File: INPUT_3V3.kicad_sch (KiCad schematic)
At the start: 3 parts

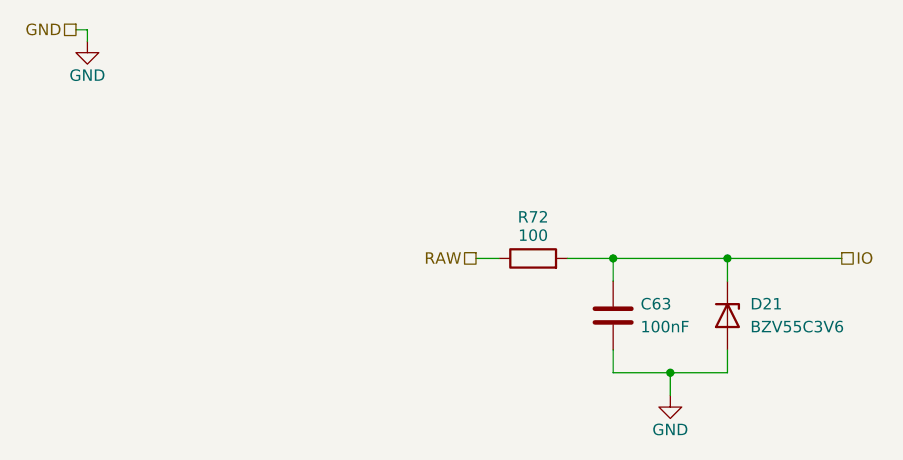
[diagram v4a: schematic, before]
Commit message: redid annotations, added test point
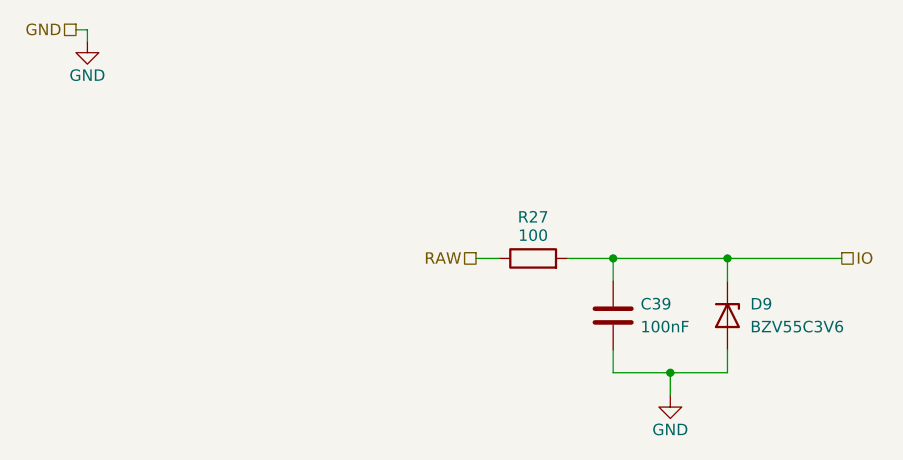
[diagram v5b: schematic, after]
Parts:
- renumbered C63 to C39, D21 to D9, R72 to R27
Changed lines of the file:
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@@
 		(on_board yes)
 		(dnp no)
-		(property "Reference" "#PWR0226"
+		(property "Reference" "#PWR0174"
 			(at 91.44 72.39 0)
 			(effects
@@
 			(project "NCU"
 				(path "/3aee14c3-5480-4f7c-989e-3fef81779034/cc997df9-87ce-41ac-9f91-f99587d0a3ba/1ff2a418-0502-41ce-a944-c34eeb1f8dd3"
-					(reference "#PWR0229")
-					(unit 1)
-				)
-				(path "/3aee14c3-5480-4f7c-989e-3fef81779034/cc997df9-87ce-41ac-9f91-f99587d0a3ba/8349b2b4-bb6e-4977-8ad0-8673fa6e8690"
-					(reference "#PWR0224")
-					(unit 1)
-				)
-				(path "/3aee14c3-5480-4f7c-989e-3fef81779034/cc997df9-87ce-41ac-9f91-f99587d0a3ba/901b76bf-7cf9-4caa-a7a4-13e1918a1e45"
-					(reference "#PWR0233")
-					(unit 1)
-				)
-				(path "/3aee14c3-5480-4f7c-989e-3fef81779034/cc997df9-87ce-41ac-9f91-f99587d0a3ba/c04eb7e9-4d6a-4342-82ea-b2612a59e00a"
-					(reference "#PWR0226")
+					(reference "#PWR0176")
+					(unit 1)
+				)
+				(path "/3aee14c3-5480-4f7c-989e-3fef81779034/cc997df9-87ce-41ac-9f91-f99587d0a3ba/8349b2b4-bb6e-4977-8ad0-8673fa6e8690"
+					(reference "#PWR0257")
+					(unit 1)
+				)
+				(path "/3aee14c3-5480-4f7c-989e-3fef81779034/cc997df9-87ce-41ac-9f91-f99587d0a3ba/901b76bf-7cf9-4caa-a7a4-13e1918a1e45"
+					(reference "#PWR0235")
+					(unit 1)
+				)
+				(path "/3aee14c3-5480-4f7c-989e-3fef81779034/cc997df9-87ce-41ac-9f91-f99587d0a3ba/c04eb7e9-4d6a-4342-82ea-b2612a59e00a"
+					(reference "#PWR0174")
 					(unit 1)
 				)
@@
 		(on_board yes)
 		(dnp no)
-		(property "Reference" "#PWR0225"
+		(property "Reference" "#PWR0173"
 			(at 26.67 33.02 0)
 			(effects
@@
 			(project "NCU"
 				(path "/3aee14c3-5480-4f7c-989e-3fef81779034/cc997df9-87ce-41ac-9f91-f99587d0a3ba/1ff2a418-0502-41ce-a944-c34eeb1f8dd3"
-					(reference "#PWR0228")
-					(unit 1)
-				)
-				(path "/3aee14c3-5480-4f7c-989e-3fef81779034/cc997df9-87ce-41ac-9f91-f99587d0a3ba/8349b2b4-bb6e-4977-8ad0-8673fa6e8690"
-					(reference "#PWR0222")
-					(unit 1)
-				)
-				(path "/3aee14c3-5480-4f7c-989e-3fef81779034/cc997df9-87ce-41ac-9f91-f99587d0a3ba/901b76bf-7cf9-4caa-a7a4-13e1918a1e45"
-					(reference "#PWR0232")
-					(unit 1)
-				)
-				(path "/3aee14c3-5480-4f7c-989e-3fef81779034/cc997df9-87ce-41ac-9f91-f99587d0a3ba/c04eb7e9-4d6a-4342-82ea-b2612a59e00a"
-					(reference "#PWR0225")
+					(reference "#PWR0175")
+					(unit 1)
+				)
+				(path "/3aee14c3-5480-4f7c-989e-3fef81779034/cc997df9-87ce-41ac-9f91-f99587d0a3ba/8349b2b4-bb6e-4977-8ad0-8673fa6e8690"
+					(reference "#PWR0256")
+					(unit 1)
+				)
+				(path "/3aee14c3-5480-4f7c-989e-3fef81779034/cc997df9-87ce-41ac-9f91-f99587d0a3ba/901b76bf-7cf9-4caa-a7a4-13e1918a1e45"
+					(reference "#PWR0234")
+					(unit 1)
+				)
+				(path "/3aee14c3-5480-4f7c-989e-3fef81779034/cc997df9-87ce-41ac-9f91-f99587d0a3ba/c04eb7e9-4d6a-4342-82ea-b2612a59e00a"
+					(reference "#PWR0173")
 					(unit 1)
 				)
@@
 		(dnp no)
 		(fields_autoplaced yes)
-		(property "Reference" "D21"
+		(property "Reference" "D9"
 			(at 100.33 55.8799 90)
 			(effects
@@
 			(project "NCU"
 				(path "/3aee14c3-5480-4f7c-989e-3fef81779034/cc997df9-87ce-41ac-9f91-f99587d0a3ba/1ff2a418-0502-41ce-a944-c34eeb1f8dd3"
-					(reference "D22")
-					(unit 1)
-				)
-				(path "/3aee14c3-5480-4f7c-989e-3fef81779034/cc997df9-87ce-41ac-9f91-f99587d0a3ba/8349b2b4-bb6e-4977-8ad0-8673fa6e8690"
+					(reference "D10")
+					(unit 1)
+				)
+				(path "/3aee14c3-5480-4f7c-989e-3fef81779034/cc997df9-87ce-41ac-9f91-f99587d0a3ba/8349b2b4-bb6e-4977-8ad0-8673fa6e8690"
+					(reference "D25")
+					(unit 1)
+				)
+				(path "/3aee14c3-5480-4f7c-989e-3fef81779034/cc997df9-87ce-41ac-9f91-f99587d0a3ba/901b76bf-7cf9-4caa-a7a4-13e1918a1e45"
 					(reference "D20")
 					(unit 1)
 				)
-				(path "/3aee14c3-5480-4f7c-989e-3fef81779034/cc997df9-87ce-41ac-9f91-f99587d0a3ba/901b76bf-7cf9-4caa-a7a4-13e1918a1e45"
-					(reference "D23")
-					(unit 1)
-				)
-				(path "/3aee14c3-5480-4f7c-989e-3fef81779034/cc997df9-87ce-41ac-9f91-f99587d0a3ba/c04eb7e9-4d6a-4342-82ea-b2612a59e00a"
-					(reference "D21")
+				(path "/3aee14c3-5480-4f7c-989e-3fef81779034/cc997df9-87ce-41ac-9f91-f99587d0a3ba/c04eb7e9-4d6a-4342-82ea-b2612a59e00a"
+					(reference "D9")
 					(unit 1)
 				)
@@
 		(on_board yes)
 		(dnp no)
-		(property "Reference" "R72"
+		(property "Reference" "R27"
 			(at 76.2 46.228 90)
 			(effects
@@
 			(project "NCU"
 				(path "/3aee14c3-5480-4f7c-989e-3fef81779034/cc997df9-87ce-41ac-9f91-f99587d0a3ba/1ff2a418-0502-41ce-a944-c34eeb1f8dd3"
-					(reference "R73")
-					(unit 1)
-				)
-				(path "/3aee14c3-5480-4f7c-989e-3fef81779034/cc997df9-87ce-41ac-9f91-f99587d0a3ba/8349b2b4-bb6e-4977-8ad0-8673fa6e8690"
-					(reference "R71")
-					(unit 1)
-				)
-				(path "/3aee14c3-5480-4f7c-989e-3fef81779034/cc997df9-87ce-41ac-9f91-f99587d0a3ba/901b76bf-7cf9-4caa-a7a4-13e1918a1e45"
-					(reference "R74")
-					(unit 1)
-				)
-				(path "/3aee14c3-5480-4f7c-989e-3fef81779034/cc997df9-87ce-41ac-9f91-f99587d0a3ba/c04eb7e9-4d6a-4342-82ea-b2612a59e00a"
+					(reference "R28")
+					(unit 1)
+				)
+				(path "/3aee14c3-5480-4f7c-989e-3fef81779034/cc997df9-87ce-41ac-9f91-f99587d0a3ba/8349b2b4-bb6e-4977-8ad0-8673fa6e8690"
 					(reference "R72")
+					(unit 1)
+				)
+				(path "/3aee14c3-5480-4f7c-989e-3fef81779034/cc997df9-87ce-41ac-9f91-f99587d0a3ba/901b76bf-7cf9-4caa-a7a4-13e1918a1e45"
+					(reference "R60")
+					(unit 1)
+				)
+				(path "/3aee14c3-5480-4f7c-989e-3fef81779034/cc997df9-87ce-41ac-9f91-f99587d0a3ba/c04eb7e9-4d6a-4342-82ea-b2612a59e00a"
+					(reference "R27")
 					(unit 1)
 				)
@@
 		(on_board yes)
 		(dnp no)
-		(property "Reference" "C63"
+		(property "Reference" "C39"
 			(at 88.138 55.88 0)
 			(effects
@@
 			(project "NCU"
 				(path "/3aee14c3-5480-4f7c-989e-3fef81779034/cc997df9-87ce-41ac-9f91-f99587d0a3ba/1ff2a418-0502-41ce-a944-c34eeb1f8dd3"
-					(reference "C64")
-					(unit 1)
-				)
-				(path "/3aee14c3-5480-4f7c-989e-3fef81779034/cc997df9-87ce-41ac-9f91-f99587d0a3ba/8349b2b4-bb6e-4977-8ad0-8673fa6e8690"
-					(reference "C62")
-					(unit 1)
-				)
-				(path "/3aee14c3-5480-4f7c-989e-3fef81779034/cc997df9-87ce-41ac-9f91-f99587d0a3ba/901b76bf-7cf9-4caa-a7a4-13e1918a1e45"
-					(reference "C65")
-					(unit 1)
-				)
-				(path "/3aee14c3-5480-4f7c-989e-3fef81779034/cc997df9-87ce-41ac-9f91-f99587d0a3ba/c04eb7e9-4d6a-4342-82ea-b2612a59e00a"
+					(reference "C40")
+					(unit 1)
+				)
+				(path "/3aee14c3-5480-4f7c-989e-3fef81779034/cc997df9-87ce-41ac-9f91-f99587d0a3ba/8349b2b4-bb6e-4977-8ad0-8673fa6e8690"
 					(reference "C63")
 					(unit 1)
 				)
+				(path "/3aee14c3-5480-4f7c-989e-3fef81779034/cc997df9-87ce-41ac-9f91-f99587d0a3ba/901b76bf-7cf9-4caa-a7a4-13e1918a1e45"
+					(reference "C58")
+					(unit 1)
+				)
+				(path "/3aee14c3-5480-4f7c-989e-3fef81779034/cc997df9-87ce-41ac-9f91-f99587d0a3ba/c04eb7e9-4d6a-4342-82ea-b2612a59e00a"
+					(reference "C39")
+					(unit 1)
+				)
